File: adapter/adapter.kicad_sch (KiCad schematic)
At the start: 2 parts, among them J1 FlipperGPIO, U1 CC1101_Connector

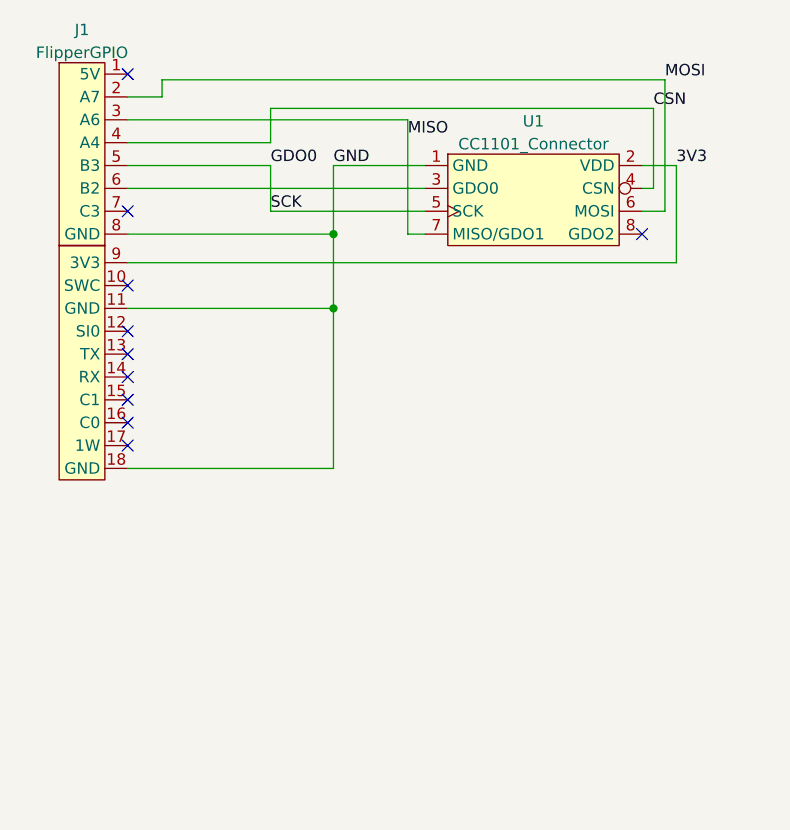
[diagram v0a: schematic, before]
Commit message: include a 5V to 3.3V buck converter for more reliable power supply update to include a power LED since 5V is not always active
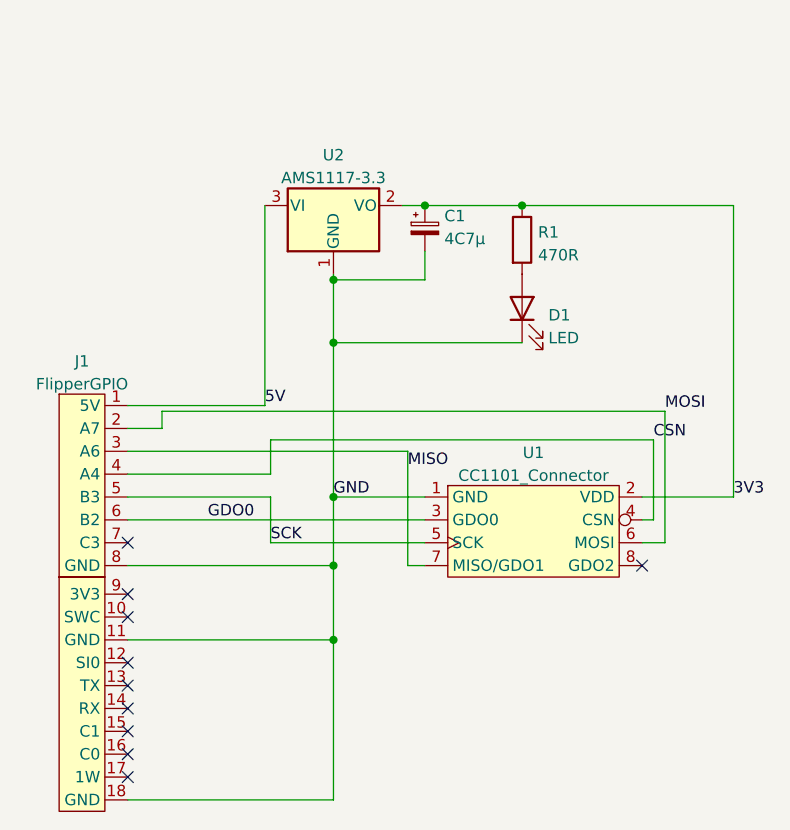
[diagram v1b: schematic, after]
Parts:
- added C1: 4C7µ, Capacitor_THT:CP_Radial_D4.0mm_P2.00mm, symbol Device:C_Polarized_Small
- added D1: LED, LED_THT:LED_D3.0mm, symbol Device:LED
- added R1: 470R, Resistor_THT:R_Axial_DIN0207_L6.3mm_D2.5mm_P7.62mm_Horizontal, symbol Device:R
- added U2: AMS1117-3.3, Connector_PinHeader_2.54mm:PinHeader_1x03_P2.54mm_Vertical, symbol Regulator_Linear:AMS1117-3.3
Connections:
- net 3V3: now also C1.1, R1.1, U2.2 (VO); no longer J1.9 (3V3)
- net GDO0: now also J1.6 (B2), U1.3 (GDO0); no longer J1.5 (B3), U1.5 (SCK)
- net GND: now also C1.2, D1.1 (K), U2.1 (GND)
- net 5V: now reaches J1.1 (5V)
- net 5V: now also U2.3 (VI)
- new net: D1.2 (A), R1.2
- new net SCK: J1.5 (B3), U1.5 (SCK)
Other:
- moved on the sheet: J1, U1
